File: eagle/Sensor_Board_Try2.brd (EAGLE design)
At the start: 69.8 x 64.4 mm, 32 parts, among them IC1 AT24CP, IC3 DS1307, Q1 BSS123, Q2 BSS123, Q3 32.768

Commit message: few changes to the board
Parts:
- removed C2, C3: 12.5pF, eagle-ltspice:C0805
- removed C4, C5: (no value), rcl:E2-4
- removed G1: 10MM_SM_COIN_CELL_CLIP, battery:10MM_SM_COIN_CELL_CLIP
- removed R13: 10k, rcl:M0805
- removed R14, R9: 4.7k, rcl:M0805
- added R12: 4.7K, adafruit:M1406
- added R4: 10K, resistor:M1406
- added R5: 10k, rcl:M1406
- added R8: 4.7K, resistor:M1406
- JP2: value JP2 -> JUMPER-SMT_3_1-NC_TRACE_SILK
- JP3: value JP3 -> JUMPER-SMT_3_1-NC_TRACE_SILK
- JP4: value JP4 -> JUMPER-SMT_3_1-NC_TRACE_SILK
- R1, R2, R3: value 10k -> 10K; device rcl:M0805 -> resistor:M1406
- R11: value 10k -> 4.7K; device rcl:M0805 -> adafruit:M1406
- R6, R7: value 4.7k -> 4.7K; device rcl:M0805 -> resistor:M1406
- moved J4 63.1 mm to (16.5, 59.7), turned to 0 degrees
- moved J2 59.6 mm to (26.7, 59.7), turned to 0 degrees
- moved J5 58.2 mm to (11.4, 43.2), turned to 90 degrees
- moved R7 57.1 mm to (19.1, 53.3), turned to 270 degrees
- moved R6 50.8 mm to (29.2, 53.3), turned to 270 degrees
- moved R11 40.4 mm to (68.6, 31.8), turned to 270 degrees
- moved IC3 29.0 mm to (54.6, 40.6)
- moved SV3 26.6 mm to (63.5, 31.8), turned to 90 degrees
- moved J3 24.0 mm to (26.7, 2.54), turned to 90 degrees
- moved SV1 23.9 mm to (57.1, 55.9), turned to 0 degrees
- moved R3 22.5 mm to (29.2, 29.2)
- moved Q3 19.4 mm to (49.5, 31.8), turned to 270 degrees
- moved Q1 18.4 mm to (38.1, 29.2)
- moved IC1 17.8 mm to (17.8, 27.9), turned to 270 degrees
- moved R2 17.6 mm to (44.5, 38.1), turned to 270 degrees
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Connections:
- net 3V: now also R1.2, R3.2; no longer C5.+, R11.2, R2.2
- net 5V: now also R11.1, R12.2, R2.2, R4.2, R5.1, R8.2; no longer C4.+, R1.2, R13.2, R14.2, R3.2, R9.2
- net GND: no longer C2.2, C3.2, C4.-, C5.-, G1.-
- net N$14: no longer C2.1
- net N$15: no longer C3.1
- net N$6: no longer G1.+@1, G1.+@2
- net PD5: now also R6.1; no longer R9.1
- net PD6: now also R7.1; no longer R6.1
- net PD7: now also R8.1; no longer R7.1
- net RESET: now also R5.2; no longer R13.1
- net SCL: now also R11.2, R4.1; no longer R3.1
- net SCLL: now also R3.1; no longer R2.1
- net SDA: now also R12.1, R2.1; no longer R1.1
- net SDAL: now also R1.1; no longer R11.1
- net SQW: no longer R14.1
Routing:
- net 5V: track 128.6 -> 214.6 mm, vias 2 -> 0
- net 3V: track 118.5 -> 201.3 mm
- net PD7: track 16.8 -> 74.9 mm
- net PD6: track 15.6 -> 66.0 mm
- net SDA: track 63.7 -> 105.2 mm
- net PD5: track 15.0 -> 55.4 mm
- net SCL: track 63.5 -> 100.7 mm, vias 2 -> 1
- net SDAL: track 45.8 -> 74.4 mm, vias 2 -> 0
- net RESET: track 19.5 -> 36.7 mm
- net GND: track 16.9 -> 0.00 mm, vias 5 -> 0
- net SCLL: track 46.1 -> 34.4 mm
- net N$14: track 6.11 -> 17.8 mm
- net SQW: track 9.31 -> 0.00 mm
- net N$15: track 6.05 -> 15.2 mm
- net N$6: track 6.75 -> 0.00 mm
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
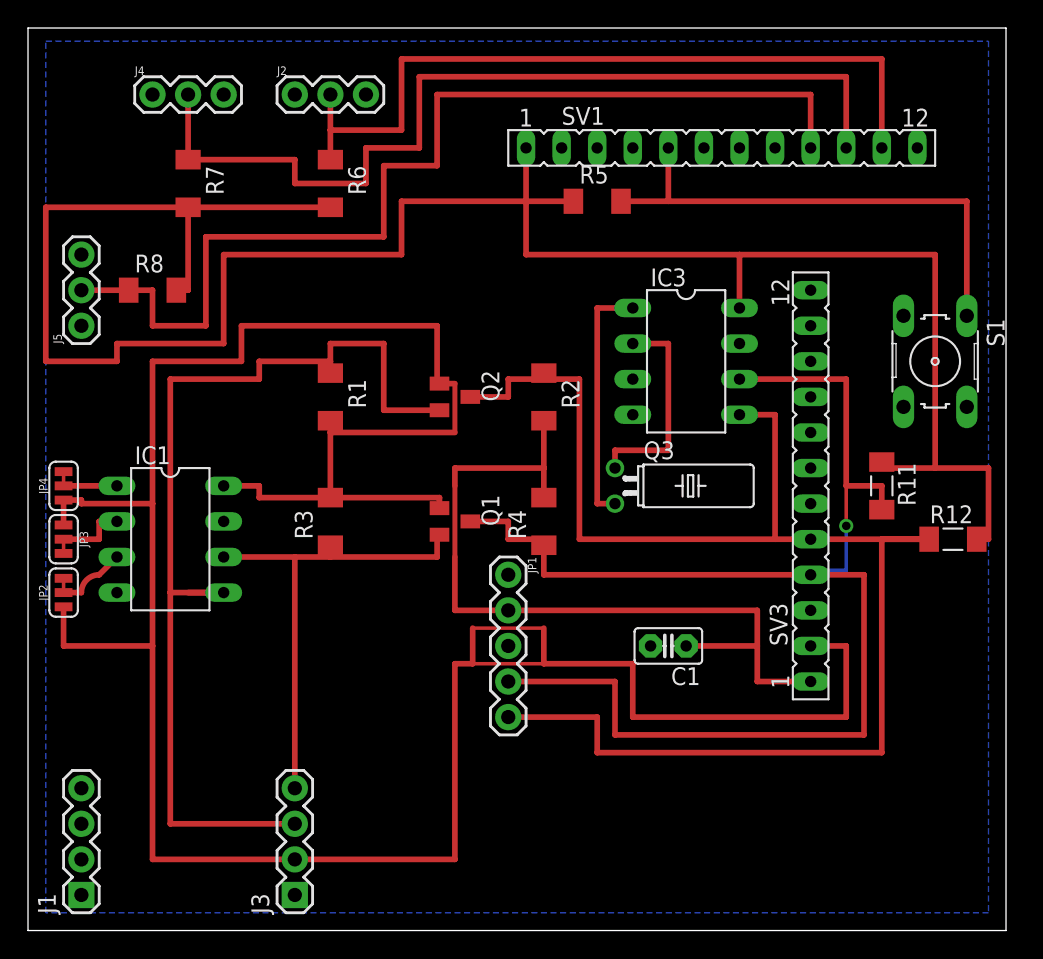
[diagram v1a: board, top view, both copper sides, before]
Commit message: moved the boards into eagle folder
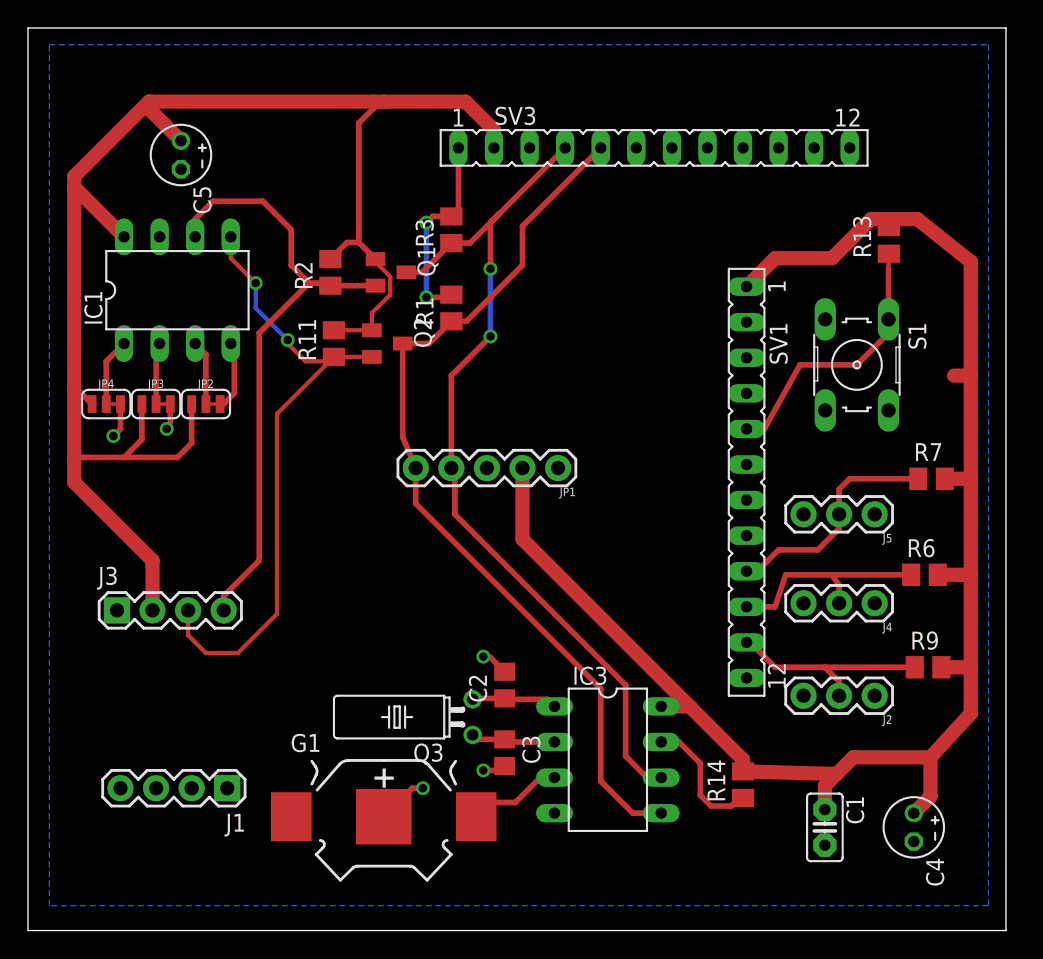
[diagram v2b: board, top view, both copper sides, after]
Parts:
- removed R12: 4.7K, adafruit:M1406
- removed R4: 10K, resistor:M1406
- removed R5: 10k, rcl:M1406
- removed R8: 4.7K, resistor:M1406
- added C2, C3: 12.5pF, eagle-ltspice:C0805
- added C4, C5: (no value), rcl:E2-4
- added G1: 10MM_SM_COIN_CELL_CLIP, battery:10MM_SM_COIN_CELL_CLIP
- added R13: 10k, rcl:M0805
- added R14, R9: 4.7k, rcl:M0805
- JP2: value JUMPER-SMT_3_1-NC_TRACE_SILK -> JP2
- JP3: value JUMPER-SMT_3_1-NC_TRACE_SILK -> JP3
- JP4: value JUMPER-SMT_3_1-NC_TRACE_SILK -> JP4
- R1, R2, R3: value 10K -> 10k; device resistor:M1406 -> rcl:M0805
- R11: value 4.7K -> 10k; device adafruit:M1406 -> rcl:M0805
- R6, R7: value 4.7K -> 4.7k; device resistor:M1406 -> rcl:M0805
- moved J4 63.1 mm to (68.1, 23.4), turned to 180 degrees
- moved J2 59.6 mm to (68.1, 16.8), turned to 180 degrees
- moved J5 58.2 mm to (68.1, 29.7), turned to 180 degrees
- moved R7 57.1 mm to (72.1, 32.3), turned to 0 degrees
- moved R6 50.8 mm to (71.6, 25.4), turned to 0 degrees
- moved R11 40.4 mm to (29.5, 41.9), turned to 90 degrees
- moved IC3 29.0 mm to (49.0, 12.2)
- moved SV3 26.6 mm to (52.3, 55.9), turned to 0 degrees
- moved J3 24.0 mm to (14.0, 22.9), turned to 0 degrees
- moved SV1 23.9 mm to (58.9, 32.0), turned to 270 degrees
- moved R3 22.5 mm to (37.8, 50.0)
- moved Q3 19.4 mm to (39.4, 15.2), turned to 90 degrees
- moved Q1 18.4 mm to (33.5, 47.0)
- moved IC1 17.8 mm to (18.3, 45.7), turned to 0 degrees
- moved R2 17.6 mm to (29.2, 47.0), turned to 90 degrees
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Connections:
- removed net N$6: IC3.3
- new net VBAT: G1.+@1, G1.+@2, IC3.3
- net 3V: now also C5.+, R11.2, R2.2; no longer R1.2, R3.2
- net 5V: now also C4.+, R1.2, R13.2, R14.2, R3.2, R9.2; no longer R11.1, R12.2, R2.2, R4.2, R5.1, R8.2
- net GND: now also C2.2, C3.2, C4.-, C5.-, G1.-
- net N$14: now also C2.1
- net N$15: now also C3.1
- net PD5: now also R9.1; no longer R6.1
- net PD6: now also R6.1; no longer R7.1
- net PD7: now also R7.1; no longer R8.1
- net RESET: now also R13.1; no longer R5.2
- net SCL: now also R3.1; no longer R11.2, R4.1
- net SCLL: now also R2.1; no longer R3.1
- net SDA: now also R1.1; no longer R12.1, R2.1
- net SDAL: now also R11.1; no longer R1.1
- net SQW: now also R14.1
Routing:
- net 5V: track 214.6 -> 128.6 mm, vias 0 -> 2
- net 3V: track 201.3 -> 118.5 mm
- net PD7: track 74.9 -> 16.8 mm
- net PD6: track 66.0 -> 15.6 mm
- net SDA: track 105.2 -> 63.7 mm
- net PD5: track 55.4 -> 15.0 mm
- net SCL: track 100.7 -> 63.5 mm, vias 1 -> 2
- net SDAL: track 74.4 -> 45.8 mm, vias 0 -> 2
- net RESET: track 36.7 -> 19.5 mm
- net GND: track 0.00 -> 16.9 mm, vias 0 -> 5
- net SCLL: track 34.4 -> 46.1 mm
- net N$14: track 17.8 -> 6.11 mm
- net SQW: track 0.00 -> 9.31 mm
- net N$15: track 15.2 -> 6.05 mm
- net VBAT: track 0.00 -> 6.75 mm
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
